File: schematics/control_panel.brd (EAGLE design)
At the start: 62.1 x 66 mm, 44 parts, among them J1 AVR_SPI_PRG_6NS, Q1 L78M05CDT, U1 LTC4412ES6TRMPBF, U2 NX2301P, U3 NX2301P

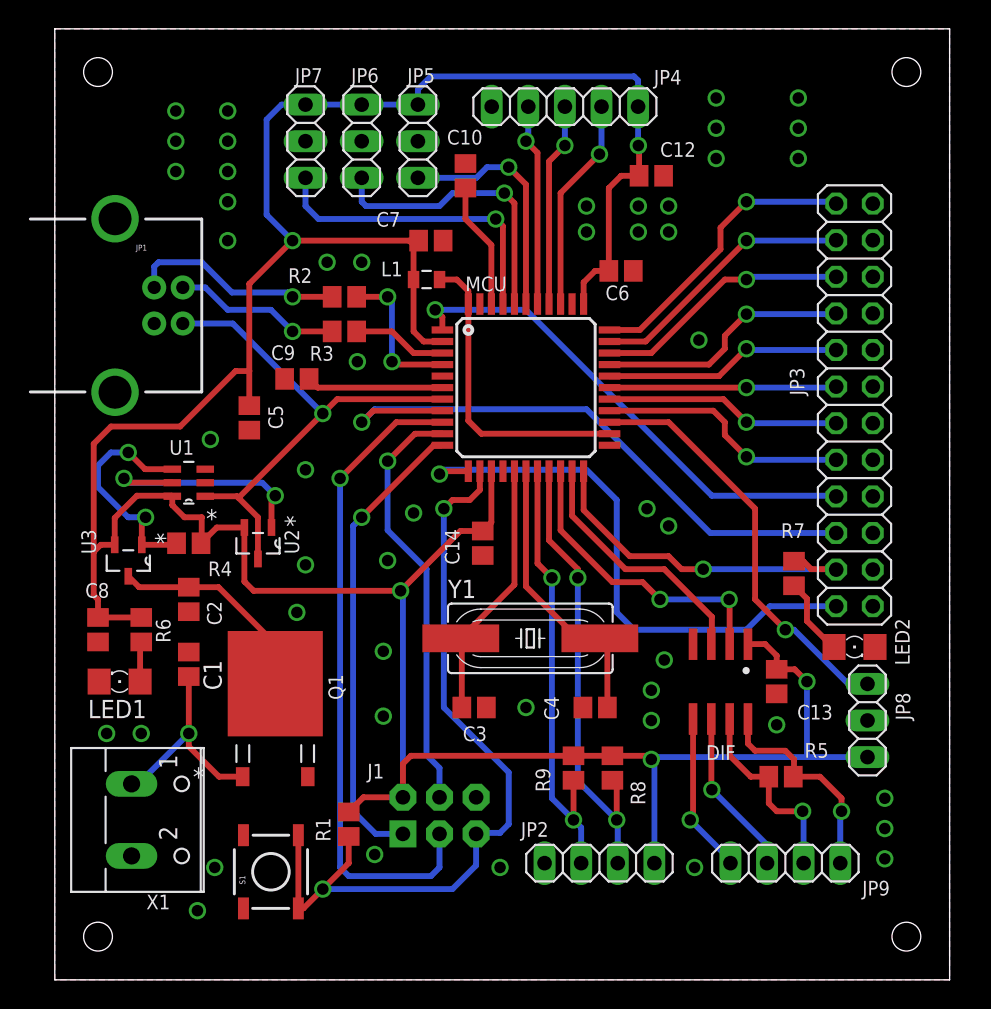
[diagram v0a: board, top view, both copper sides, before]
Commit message: Widened supply traces.
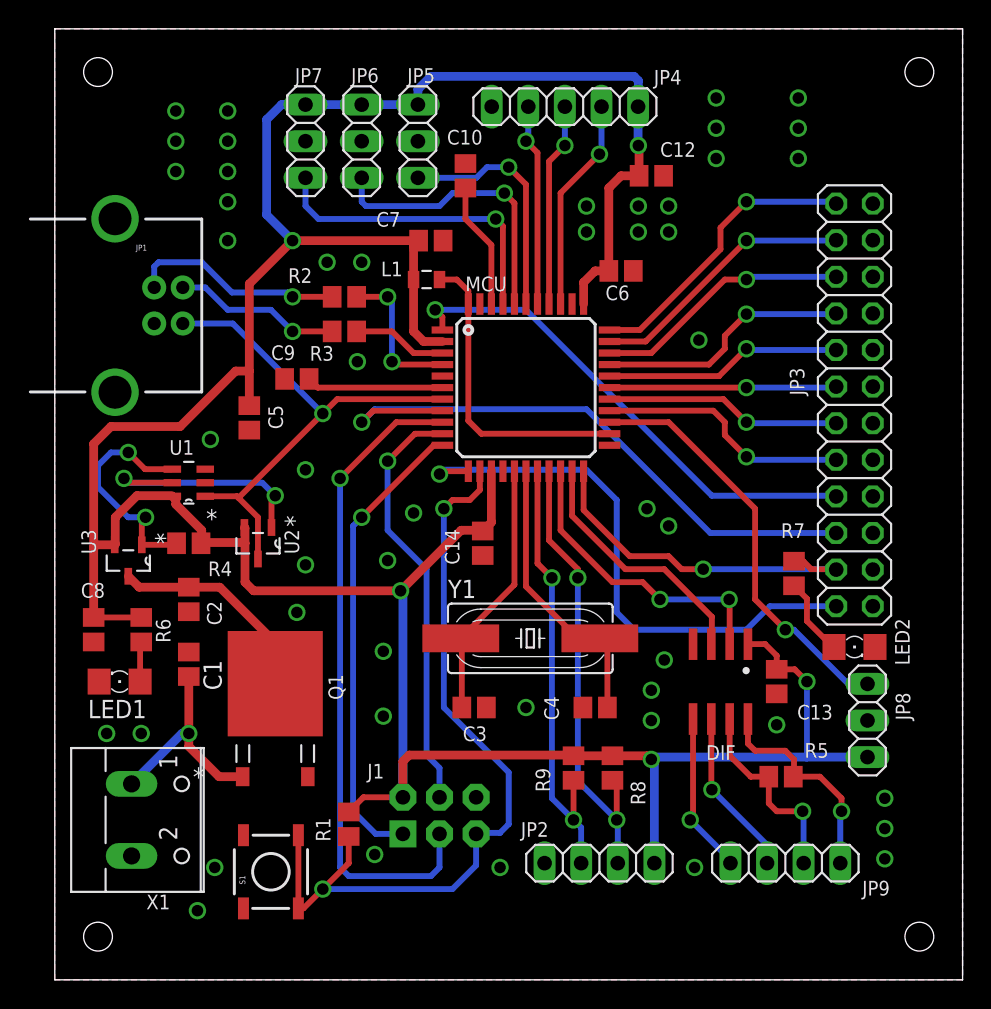
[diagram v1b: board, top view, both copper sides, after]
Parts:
- moved C8 0.30 mm to (2.70, 24.3)
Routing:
- net VCC: track 228.5 -> 227.6 mm
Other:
- board size 62.1 x 66 mm -> 63 x 66 mm
